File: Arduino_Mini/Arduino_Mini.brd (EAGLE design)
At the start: 63.1 x 23.1 mm, 31 parts, among them J1 4P-SMD-2.0-90D, J2 AIN/I2C, J3 4P-SMD-2.0-90D, J4 4P-SMD-2.0-90D

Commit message: Finish Arduino Mini
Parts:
- moved SJ1 9.22 mm to (28.2, 6.10)
- moved SJ2 9.22 mm to (28.2, 9.02)
- moved SJ3 9.19 mm to (28.2, 11.9)
- moved C1 2.57 mm to (1.98, 5.84)
- moved MCP1703 2.53 mm to (6.35, 16.5)
- moved XTAL1 2.34 mm to (7.09, 11.0)
- moved W25X40CLSNIG-ND 2.33 mm to (25.9, 8.00), turned to 270 degrees
- moved C2 2.09 mm to (3.15, 16.0), turned to 270 degrees
- moved C3 1.94 mm to (3.25, 10.9)
- moved U$8 1.66 mm to (15.4, 11.4)
- moved C6 1.57 mm to (5.21, 5.84)
- moved ATMEGA328 0.74 mm to (16.3, 12.4)
- moved R1 0.64 mm to (8.48, 5.79)
- moved C5 0.63 mm to (23.7, 13.1)
- moved C4 0.40 mm to (11.4, 5.82)
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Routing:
- net GND: track 209.7 -> 149.0 mm, vias 8 -> 11
- net A4_SDA: track 86.3 -> 40.5 mm, vias 4 -> 1
- net D11_MOSI: track 73.7 -> 32.5 mm, vias 7 -> 3
- net D12_MISO: track 67.3 -> 34.3 mm, vias 3 -> 4
- net A0: track 51.9 -> 20.1 mm, vias 0 -> 1
- net D13_SCK: track 62.0 -> 34.7 mm, vias 0 -> 3
- net D2: track 64.9 -> 81.6 mm
- net D4: track 33.7 -> 48.1 mm, vias 3 -> 5
- net D7: track 9.83 -> 23.6 mm, vias 1 -> 0
- net RST: track 24.5 -> 35.1 mm, vias 0 -> 2
- net A5_SCL: track 37.9 -> 48.2 mm, vias 2 -> 4
- net D9: track 30.9 -> 40.9 mm, vias 0 -> 3
- net D8: track 9.24 -> 18.4 mm, vias 1 -> 0
- net A6: track 62.2 -> 70.3 mm
- net A7: track 60.6 -> 55.0 mm, vias 3 -> 6
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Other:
- outline, holes or cut-outs redrawn
- board text added: "DIO1>D7"
- board text added: "DIO2>D8"
- board text added: "RST>A0"

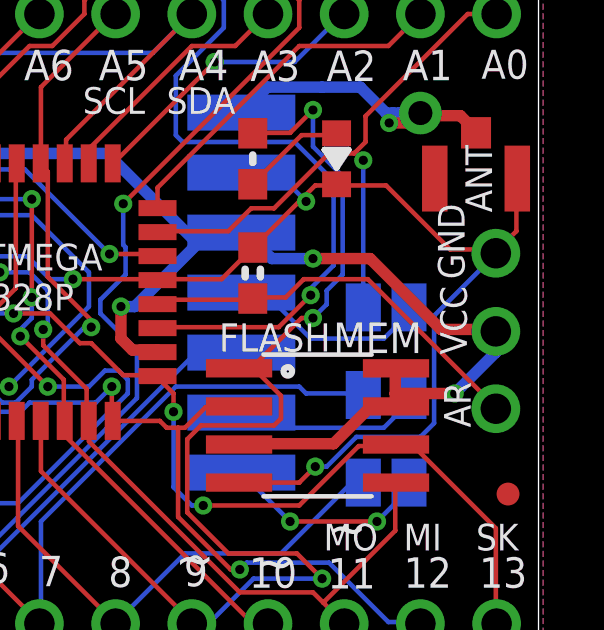
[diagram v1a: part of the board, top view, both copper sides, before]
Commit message: Correct silk for Arduino Mini
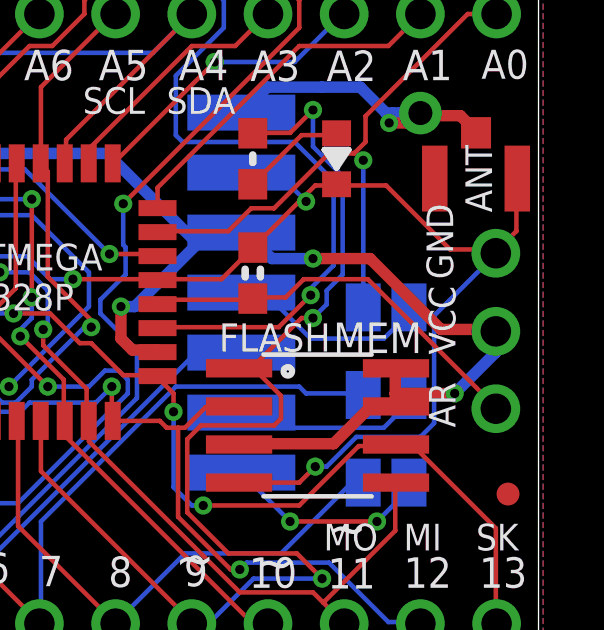
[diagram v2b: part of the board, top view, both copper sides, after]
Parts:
- R2: value 1k5 -> 1.5k
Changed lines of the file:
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@@
 <setting verticaltext="up"/>
 </settings>
-<grid distance="5" unitdist="mil" unit="mil" style="lines" multiple="1" display="yes" altdistance="1" altunitdist="mil" altunit="mil"/>
+<grid distance="5" unitdist="mil" unit="mil" style="lines" multiple="1" display="no" altdistance="1" altunitdist="mil" altunit="mil"/>
 <layers>
 <layer number="1" name="Top" color="4" fill="1" visible="yes" active="yes"/>
@@
 <board>
 <plain>
-<text x="30.1244" y="9.4488" size="0.889" layer="21" font="vector" ratio="15" rot="R270">AR</text>
+<text x="29.6164" y="9.4488" size="0.889" layer="21" font="vector" ratio="15" rot="R270">AR</text>
 <text x="5.1054" y="19.7358" size="0.889" layer="21" font="vector" ratio="15" rot="R180">VIN</text>
 <text x="-23.7744" y="9.4488" size="1.016" layer="22" font="vector" ratio="20" rot="SMR90.1">FTDI</text>
@@
 <text x="0.508" y="2.667" size="0.889" layer="21" font="vector" ratio="17">RST</text>
 <text x="0.381" y="19.558" size="0.889" layer="21" font="vector" ratio="15">GND</text>
-<text x="30.8102" y="12.8778" size="0.889" layer="21" font="vector" ratio="15" rot="R90">GND</text>
+<text x="30.4292" y="12.8778" size="0.889" layer="21" font="vector" ratio="15" rot="R90">GND</text>
 <wire x1="32.406778125" y1="23.114" x2="-28.38805" y2="23.114" width="0" layer="20"/>
 <wire x1="-28.38805" y1="23.114" x2="-29.845" y2="21.65705" width="0" layer="20" curve="90"/>
@@
 <text x="7.6454" y="19.7866" size="0.889" layer="21" font="vector" ratio="15" rot="R180">3</text>
 <text x="7.0612" y="19.7358" size="0.889" layer="21" font="vector" ratio="15" rot="R180">v</text>
-<text x="29.9974" y="12.6492" size="0.889" layer="21" font="vector" ratio="15" rot="R270">VCC</text>
+<text x="29.6164" y="12.6492" size="0.889" layer="21" font="vector" ratio="15" rot="R270">VCC</text>
 <polygon width="0.3048" layer="42">
 <vertex x="28.9814" y="19.4056"/>
@@
 <text x="-26.162" y="9.8552" size="0.889" layer="22" font="vector" ratio="15" rot="SMR90">RX</text>
 <text x="-26.162" y="12.1412" size="0.889" layer="22" font="vector" ratio="15" rot="SMR90">TX</text>
-<text x="29.9466" y="7.2136" size="0.6096" layer="22" font="vector" ratio="13" rot="MR0">DIO2&gt;D8</text>
-<text x="29.9466" y="10.1346" size="0.6096" layer="22" font="vector" ratio="13" rot="MR0">DIO1&gt;D7</text>
-<text x="29.9466" y="13.0556" size="0.6096" layer="22" font="vector" ratio="13" rot="MR0">RST&gt;A0</text>
+<text x="29.9466" y="7.2136" size="0.7112" layer="22" font="vector" ratio="15" rot="MR0">DIO2&gt;D8</text>
+<text x="29.9466" y="10.1346" size="0.7112" layer="22" font="vector" ratio="15" rot="MR0">DIO1&gt;D7</text>
+<text x="29.9466" y="13.0556" size="0.7112" layer="22" font="vector" ratio="15" rot="MR0">RST&gt;A0</text>
 </plain>
 <attributes>
@@
 <element name="ATMEGA328" library="LowPowerLab" package="TQFP32-08" value="ATMega-328" x="16.2814" y="12.446" smashed="yes"/>
 <element name="C5" library="LowPowerLab" package="0603-CAP" value="0.1" x="23.749" y="13.081" smashed="yes" rot="R90">
-<attribute name="VALUE" x="24.9047" y="15.5194" size="0.889" layer="51" font="vector" ratio="15" rot="R180"/>
+<attribute name="VALUE" x="22.1996" y="14.1097" size="0.889" layer="51" font="vector" ratio="15" rot="R270"/>
 </element>
 <element name="R1" library="LowPowerLab" package="0603-RES" value="10k" x="8.4836" y="5.7912" smashed="yes" rot="R270">
@@
 <element name="C3" library="LowPowerLab" package="0805-CAP" value="10u" x="3.2512" y="10.8966" smashed="yes" rot="R270"/>
 <element name="LED" library="LowPowerLab" package="0603-LED" value="LED0603" x="26.543" y="16.891" smashed="yes" rot="R90"/>
-<element name="R2" library="LowPowerLab" package="0603-RES" value="1k5" x="23.749" y="16.891" smashed="yes" rot="R90"/>
+<element name="R2" library="LowPowerLab" package="0603-RES" value="1.5k" x="23.749" y="16.891" smashed="yes" rot="R90">
+<attribute name="VALUE" x="23.114" y="15.748" size="0.8128" layer="27" font="vector" ratio="13" rot="R90"/>
+</element>
 <element name="U$1" library="LowPowerLab" package="RFM12B-ANTENNA" value="RFM12B_ANTENNA&quot;&quot;" x="29.337" y="18.415"/>
 <element name="W25X40CLSNIG-ND" library="LowPowerLab" package="SO08" value="AT25F512BJEDEC_3.9MM" x="25.908" y="8.001" smashed="yes" rot="R270"/>
@@
 <element name="J4" library="Seeed-Connector" library_urn="urn:adsk.eagle:library:478" package="HW4-SMD-2.0-90D" package3d_urn="urn:adsk.eagle:package:33110/1" value="4P-SMD-2.0-90D" x="-20.193" y="9.398" smashed="yes" rot="R180"/>
 <element name="FTDI1" library="LowPowerLab" package="1X06_NS_THINRINGS" value="HDR_6PINTHINRINGS" x="-28.448" y="5.207" smashed="yes" rot="R90"/>
-<element name="U$8" library="LikeCircuit" package="LORA-RA2-SMD" value="LORA-RA-02-433MHZ" x="15.367" y="11.43" smashed="yes" rot="MR0">
-<attribute name="VALUE" x="23.047" y="1.23" size="1.27" layer="28" rot="MR0"/>
-</element>
-<element name="SJ1" library="microbuilder" package="SOLDERJUMPER_REFLOW" value="" x="28.194" y="6.096" rot="MR180"/>
-<element name="SJ2" library="microbuilder" package="SOLDERJUMPER_REFLOW" value="" x="28.194" y="9.017" rot="MR180"/>
-<element name="SJ3" library="microbuilder" package="SOLDERJUMPER_REFLOW" value="" x="28.194" y="11.938" rot="MR180"/>
+<element name="U$8" library="LikeCircuit" package="LORA-RA2-SMD" value="LORA-RA-02-433MHZ" x="15.367" y="11.43" smashed="yes" rot="MR0"/>
+<element name="SJ1" library="microbuilder" package="SOLDERJUMPER_REFLOW" value="" x="28.194" y="6.096" smashed="yes" rot="MR180">
+<attribute name="NAME" x="25.654" y="5.08" size="0.7112" layer="26" font="vector" ratio="15" rot="MR90"/>
+<attribute name="VALUE" x="28.5941" y="6.096" size="0.02" layer="28" rot="MR180"/>
+</element>
+<element name="SJ2" library="microbuilder" package="SOLDERJUMPER_REFLOW" value="" x="28.194" y="9.017" smashed="yes" rot="MR180">
+<attribute name="NAME" x="25.654" y="8.128" size="0.7112" layer="26" font="vector" ratio="15" rot="MR90"/>
+<attribute name="VALUE" x="28.5941" y="9.017" size="0.02" layer="28" rot="MR180"/>
+</element>
+<element name="SJ3" library="microbuilder" package="SOLDERJUMPER_REFLOW" value="" x="28.194" y="11.938" smashed="yes" rot="MR180">
+<attribute name="NAME" x="25.527" y="10.922" size="0.7112" layer="26" font="vector" ratio="15" rot="MR90"/>
+<attribute name="VALUE" x="28.5941" y="11.938" size="0.02" layer="28" rot="MR180"/>
+</element>
 <element name="U$2" library="LowPowerLab" package="FIDUCIAL_1.5MM" value="FIDUCIAL1.5MM" x="-28.575" y="1.27"/>
 <element name="U$3" library="Anata-Symbols" package="BLOCKY_LOGO" value="" x="-1.651" y="7.493" rot="MR0"/>
